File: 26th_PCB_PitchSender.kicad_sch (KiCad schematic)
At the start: 14 parts, among them J1 Amp, J2 Conn_01x04_Pin, J3 microSD, J4 Conn_01x04_Socket, J5 BNO055, J6 BMP390

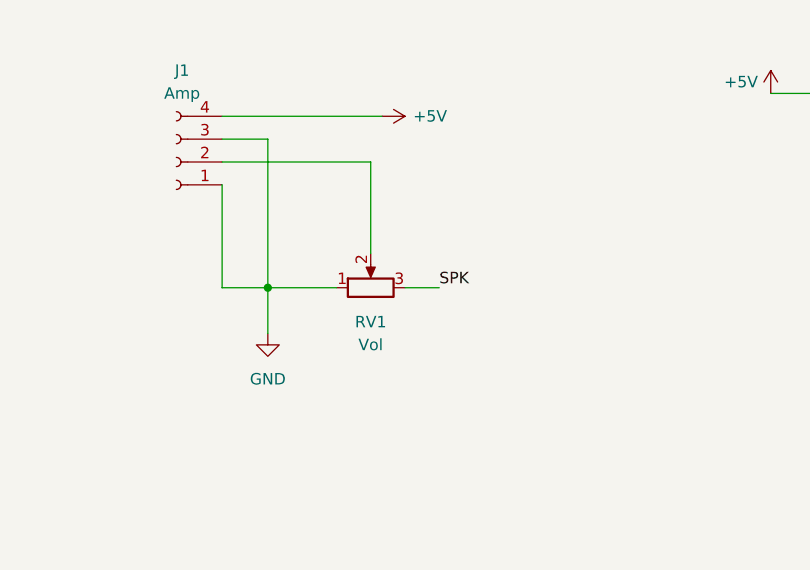
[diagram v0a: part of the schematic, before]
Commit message: Add PA connecter
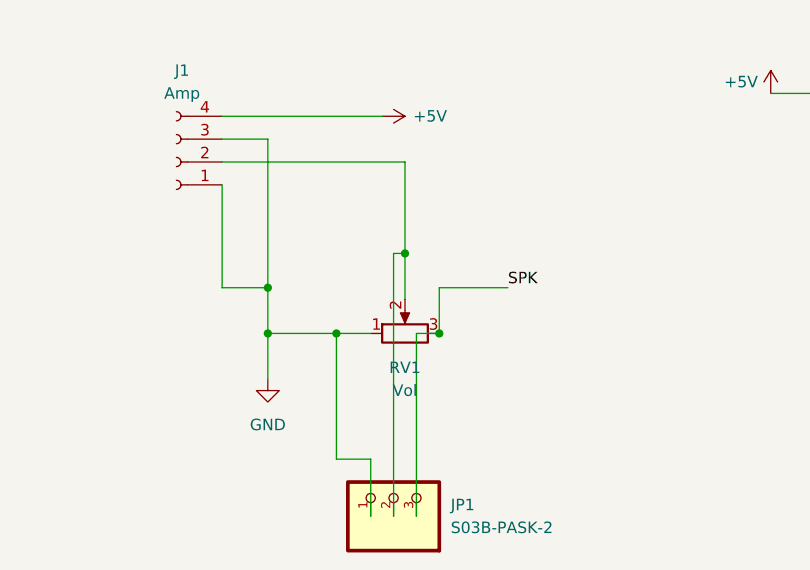
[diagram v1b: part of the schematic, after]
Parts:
- added JP1: S03B-PASK-2, lib:S03B-PASK-2, symbol S03B-PASK-2:S03B-PASK-2
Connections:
- net GND: now also JP1.1
- net SPK: now also JP1.3
- net at J1.2 (Pin_2), RV1.2: now also JP1.2
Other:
- moved on the sheet: RV1
